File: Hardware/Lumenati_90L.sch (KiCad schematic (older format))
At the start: 14 parts, among them J1 CONN_041X04_NO_SILK, J2 CONN_041X04_NO_SILK, U1 APA102, U2 APA102, U3 APA102

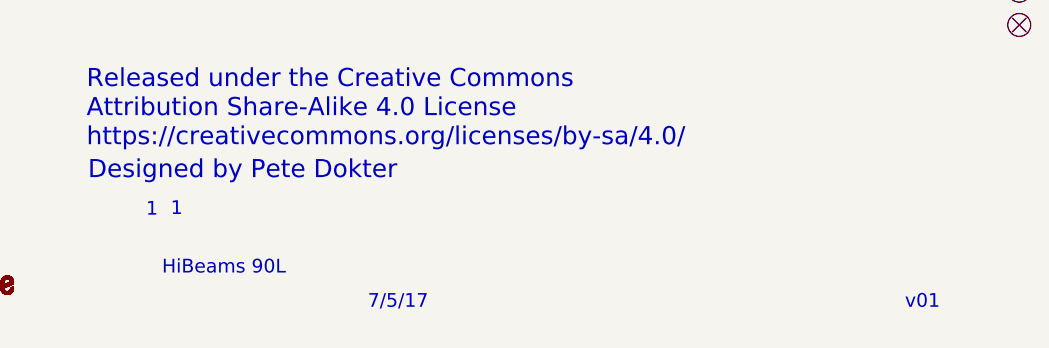
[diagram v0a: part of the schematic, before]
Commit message: Changed all the names to Lumenati, updated version to v10.
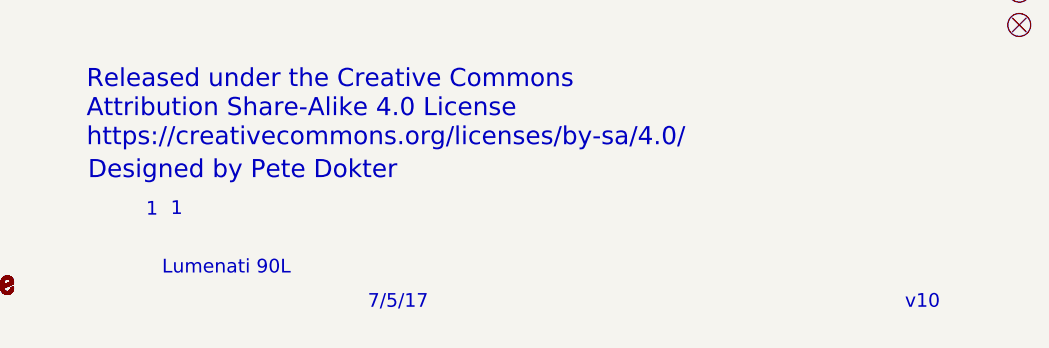
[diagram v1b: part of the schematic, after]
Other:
- note added: "Lumenati 90L"
- note added: "v10"
- note removed: "HiBeams 90L"
- note removed: "v01"
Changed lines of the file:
@@
 $EndComp
 Text Notes 10600 7650 0    60   ~ 0
-v01
+v10
 Text Notes 8250 7650 0    60   ~ 0
 7/5/17
 Text Notes 7350 7500 0    60   ~ 0
-HiBeams 90L
+Lumenati 90L
 $Comp
 L +5V #PWR04

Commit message: Added jumper description to schematic.
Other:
- note added: "Note: JP1 and JP2 are present so the user can disconnect clock and data\nsignals from subsequent boards, allowing you to make a closed loop design\nwithout having the logic from the last board interfere with the logic of the\nfirst. They are normally closed, so open them if you're making a closed\nloop design."
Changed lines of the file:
@@
 LIBS:contrib
 LIBS:valves
-LIBS:APA102
-LIBS:SparkFun-Aesthetics
-LIBS:SparkFun-Batteries
-LIBS:SparkFun-Boards
-LIBS:SparkFun-Capacitors
-LIBS:SparkFun-Clocks
-LIBS:SparkFun-Coils
-LIBS:SparkFun-Connectors
-LIBS:SparkFun-DiscreteSemi
-LIBS:SparkFun-Displays
-LIBS:SparkFun-Electromechanical
-LIBS:SparkFun-Fuses
-LIBS:SparkFun-GPS
-LIBS:SparkFun-Hardware
-LIBS:SparkFun-IC-Amplifiers
-LIBS:SparkFun-IC-Comms
-LIBS:SparkFun-IC-Conversion
-LIBS:SparkFun-IC-Logic
-LIBS:SparkFun-IC-Memory
-LIBS:SparkFun-IC-Microcontroller
-LIBS:SparkFun-IC-Power
-LIBS:SparkFun-IC-Special-Function
-LIBS:SparkFun-Jumpers
-LIBS:SparkFun-LED
-LIBS:SparkFun-PowerSymbols
-LIBS:SparkFun-Resistors
-LIBS:SparkFun-RF
-LIBS:SparkFun-Sensors
-LIBS:SparkFun-Switches
-LIBS:HiBeams_90L-cache
-EELAYER 26 0
+LIBS:Lumenati_90L-cache
+EELAYER 25 0
 EELAYER END
 $Descr A4 11693 8268
@@
 Wire Wire Line
 	8150 3350 8450 3350
+Text Notes 6300 1400 0    79   ~ 0
+Note: JP1 and JP2 are present so the user can disconnect clock and data\nsignals from subsequent boards, allowing you to make a closed loop design\nwithout having the logic from the last board interfere with the logic of the\nfirst. They are normally closed, so open them if you're making a closed\nloop design.
 $EndSCHEMATC
